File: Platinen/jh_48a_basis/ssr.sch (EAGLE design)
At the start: 6 parts, among them T1 BT136

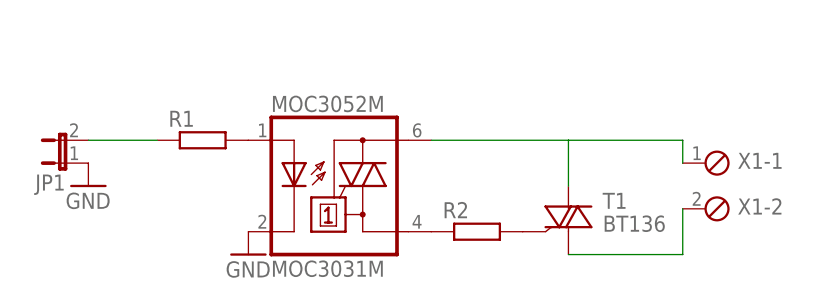
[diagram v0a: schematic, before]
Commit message: layout: update ssr board
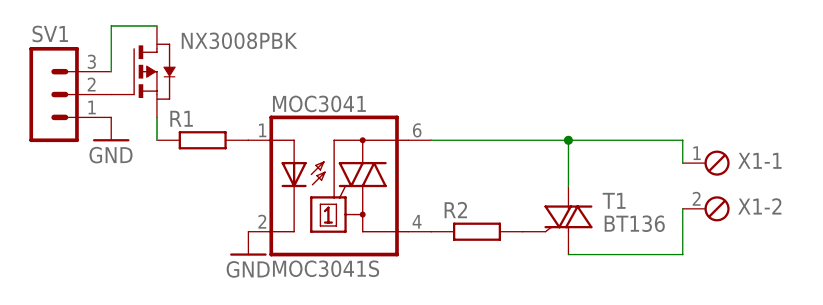
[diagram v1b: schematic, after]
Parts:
- removed JP1: (no value), jumper:JP1E
- removed MOC3052M: MOC3031M, optocoupler:MOC3031M
- added MOC3041: MOC3041S, optocoupler:MOC3041S
- added NX3008PBK: (no value), zetex:PMOSSOT23
- added SV1: (no value), con-lstb:MA03-1
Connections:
- new net N$7: NX3008PBK.G, SV1.2
- new net N$8: NX3008PBK.D, SV1.3
- net GND: now also MOC3041.C, SV1.1; no longer JP1.1, MOC3052M.C
- net N$1: now also MOC3041.A; no longer MOC3052M.A
- net N$2: now also NX3008PBK.S; no longer JP1.2
- net N$3: now also MOC3041.A1; no longer MOC3052M.A1
- net N$5: now also MOC3041.A2; no longer MOC3052M.A2
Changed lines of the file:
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@@
 <?xml version="1.0" encoding="utf-8"?>
 <!DOCTYPE eagle SYSTEM "eagle.dtd">
-<eagle version="6.3">
+<eagle version="6.2">
 <drawing>
 <settings>
@@
 </classes>
 <parts>
-<part name="MOC3052M" library="optocoupler" deviceset="MOC30*" device="" technology="31M"/>
+<part name="MOC3041" library="optocoupler" deviceset="MOC30*" device="S" technology="41">
+<attribute name="MPN" value="MOC3041S-M"/>
+<attribute name="OC_FARNELL" value="unknown"/>
+<attribute name="OC_NEWARK" value="05C2885"/>
+</part>
 <part name="R1" library="rcl" deviceset="R-EU_" device="R1206"/>
 <part name="GND1" library="supply1" deviceset="GND" device=""/>
-<part name="JP1" library="jumper" deviceset="JP1E" device=""/>
-<part name="GND2" library="supply1" deviceset="GND" device=""/>
 <part name="T1" library="triac" deviceset="BT136" device=""/>
 <part name="R2" library="rcl" deviceset="R-EU_" device="R1206"/>
 <part name="X1" library="con-phoenix-254" deviceset="MPT2" device=""/>
+<part name="NX3008PBK" library="zetex" deviceset="PMOSSOT23" device=""/>
+<part name="SV1" library="con-lstb" deviceset="MA03-1" device=""/>
+<part name="GND3" library="supply1" deviceset="GND" device=""/>
 </parts>
 <sheets>
@@
 </plain>
 <instances>
-<instance part="MOC3052M" gate="-1" x="45.72" y="40.64"/>
+<instance part="MOC3041" gate="-1" x="45.72" y="40.64"/>
 <instance part="R1" gate="G$1" x="30.48" y="45.72"/>
 <instance part="GND1" gate="1" x="35.56" y="33.02"/>
-<instance part="JP1" gate="A" x="15.24" y="43.18" rot="R90"/>
-<instance part="GND2" gate="1" x="17.78" y="40.64"/>
 <instance part="T1" gate="-1" x="71.12" y="35.56"/>
 <instance part="R2" gate="G$1" x="60.96" y="35.56"/>
 <instance part="X1" gate="-1" x="86.36" y="43.18"/>
 <instance part="X1" gate="-2" x="86.36" y="38.1"/>
+<instance part="NX3008PBK" gate="A" x="25.4" y="53.34"/>
+<instance part="SV1" gate="G$1" x="12.7" y="50.8"/>
+<instance part="GND3" gate="1" x="20.32" y="45.72"/>
 </instances>
 <busses>
@@
 <net name="N$1" class="0">
 <segment>
-<pinref part="MOC3052M" gate="-1" pin="A"/>
+<pinref part="MOC3041" gate="-1" pin="A"/>
 <pinref part="R1" gate="G$1" pin="2"/>
 </segment>
@@
 <net name="GND" class="0">
 <segment>
-<pinref part="MOC3052M" gate="-1" pin="C"/>
+<pinref part="MOC3041" gate="-1" pin="C"/>
 <pinref part="GND1" gate="1" pin="GND"/>
 </segment>
 <segment>
-<pinref part="JP1" gate="A" pin="1"/>
-<pinref part="GND2" gate="1" pin="GND"/>
+<pinref part="SV1" gate="G$1" pin="1"/>
+<pinref part="GND3" gate="1" pin="GND"/>
 </segment>
 </net>
@@
 <segment>
 <pinref part="R1" gate="G$1" pin="1"/>
-<pinref part="JP1" gate="A" pin="2"/>
-<wire x1="25.4" y1="45.72" x2="17.78" y2="45.72" width="0.1524" layer="91"/>
+<pinref part="NX3008PBK" gate="A" pin="S"/>
+<wire x1="25.4" y1="45.72" x2="25.4" y2="48.26" width="0.1524" layer="91"/>
 </segment>
 </net>
 <net name="N$3" class="0">
 <segment>
-<pinref part="MOC3052M" gate="-1" pin="A1"/>
+<pinref part="MOC3041" gate="-1" pin="A1"/>
 <pinref part="R2" gate="G$1" pin="1"/>
 </segment>
@@
 <net name="N$5" class="0">
 <segment>
-<pinref part="MOC3052M" gate="-1" pin="A2"/>
+<pinref part="MOC3041" gate="-1" pin="A2"/>
 <pinref part="T1" gate="-1" pin="A2"/>
 <wire x1="55.88" y1="45.72" x2="71.12" y2="45.72" width="0.1524" layer="91"/>
@@
 <wire x1="71.12" y1="45.72" x2="83.82" y2="45.72" width="0.1524" layer="91"/>
 <wire x1="83.82" y1="45.72" x2="83.82" y2="43.18" width="0.1524" layer="91"/>
+<junction x="71.12" y="45.72"/>
 </segment>
 </net>
@@
 </segment>
 </net>
+<net name="N$7" class="0">
+<segment>
+<pinref part="NX3008PBK" gate="A" pin="G"/>
+<pinref part="SV1" gate="G$1" pin="2"/>
+</segment>
+</net>
+<net name="N$8" class="0">
+<segment>
+<pinref part="NX3008PBK" gate="A" pin="D"/>
+<pinref part="SV1" gate="G$1" pin="3"/>
+<wire x1="25.4" y1="58.42" x2="20.32" y2="58.42" width="0.1524" layer="91"/>
+<wire x1="20.32" y1="58.42" x2="20.32" y2="53.34" width="0.1524" layer="91"/>
+</segment>
+</net>
